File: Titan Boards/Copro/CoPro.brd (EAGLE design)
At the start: 101.6 x 101.6 mm, 83 parts, among them P2 RB1-125BAG1A, Q1 310mA/60V/1.6Ω, Q10 310mA/60V/1.6Ω, Q2 310mA/60V/1.6Ω, Q3 310mA/60V/1.6Ω, Q4 310mA/60V/1.6Ω, Q5 310mA/60V/1.6Ω, Q6 310mA/60V/1.6Ω, Q7 310mA/60V/1.6Ω, Q8 310mA/60V/1.6Ω, Q9 310mA/60V/1.6Ω, U1 SN74LVC3G04DCUT, U2 SN74LVC1G11DCKR, Y1 25Mhz, Y2 12MHz, Y3 32.768kHz

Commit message: Added My President Design to Board
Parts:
- moved PROGRAMMING1 3.81 mm to (6.35, 68.8)
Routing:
- net D-: track 43.7 -> 47.5 mm
- net D+: track 43.0 -> 46.8 mm
- net +3V3: track 414.6 -> 416.1 mm, vias 27 -> 28
- net BP_SDA: track 72.6 -> 73.9 mm
- net SWCLK: track 40.5 -> 39.9 mm, vias 2 -> 4
- net SPARE_8: track 56.8 -> 56.2 mm
- net 12V_ON/OFF: vias 3 -> 5
- net +5V: vias 8 -> 10

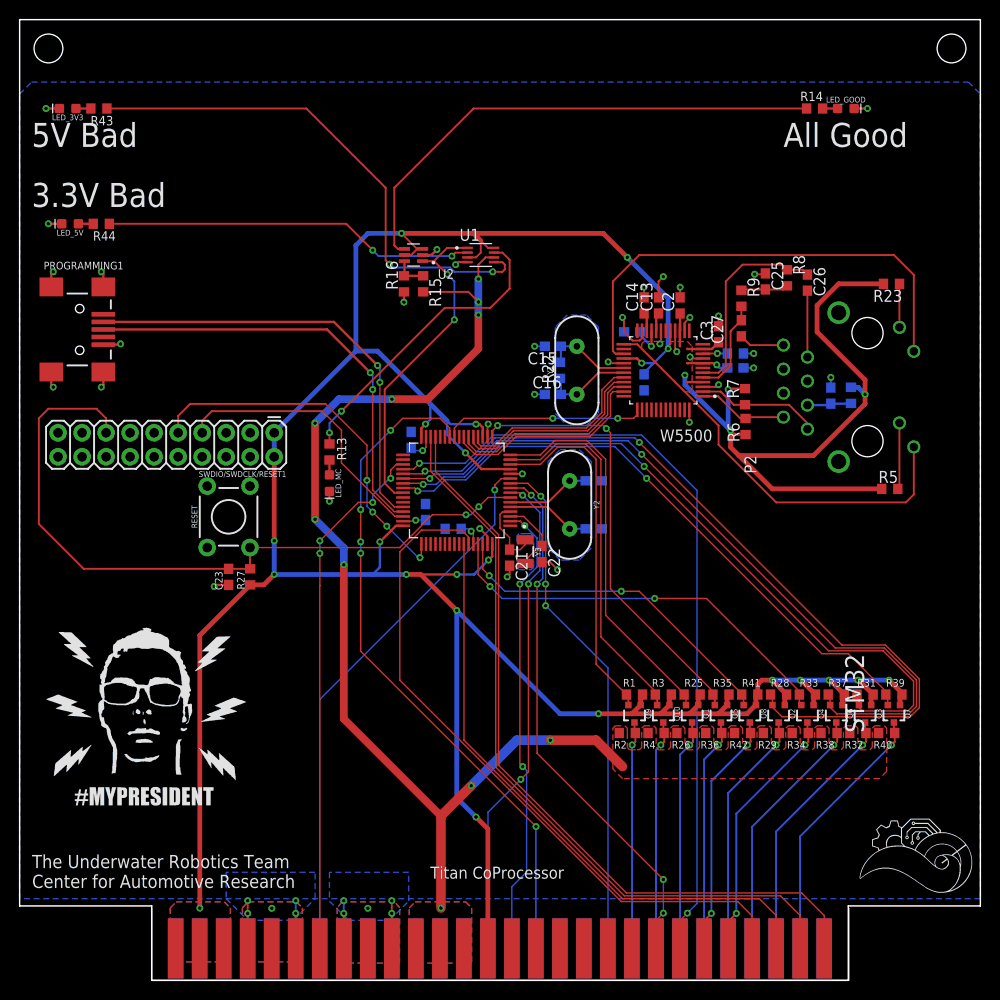
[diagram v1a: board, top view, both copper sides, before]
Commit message: CoPro - Increased some trace widths | Opened up ground plane | added decoupling capacitors to Main MicroController
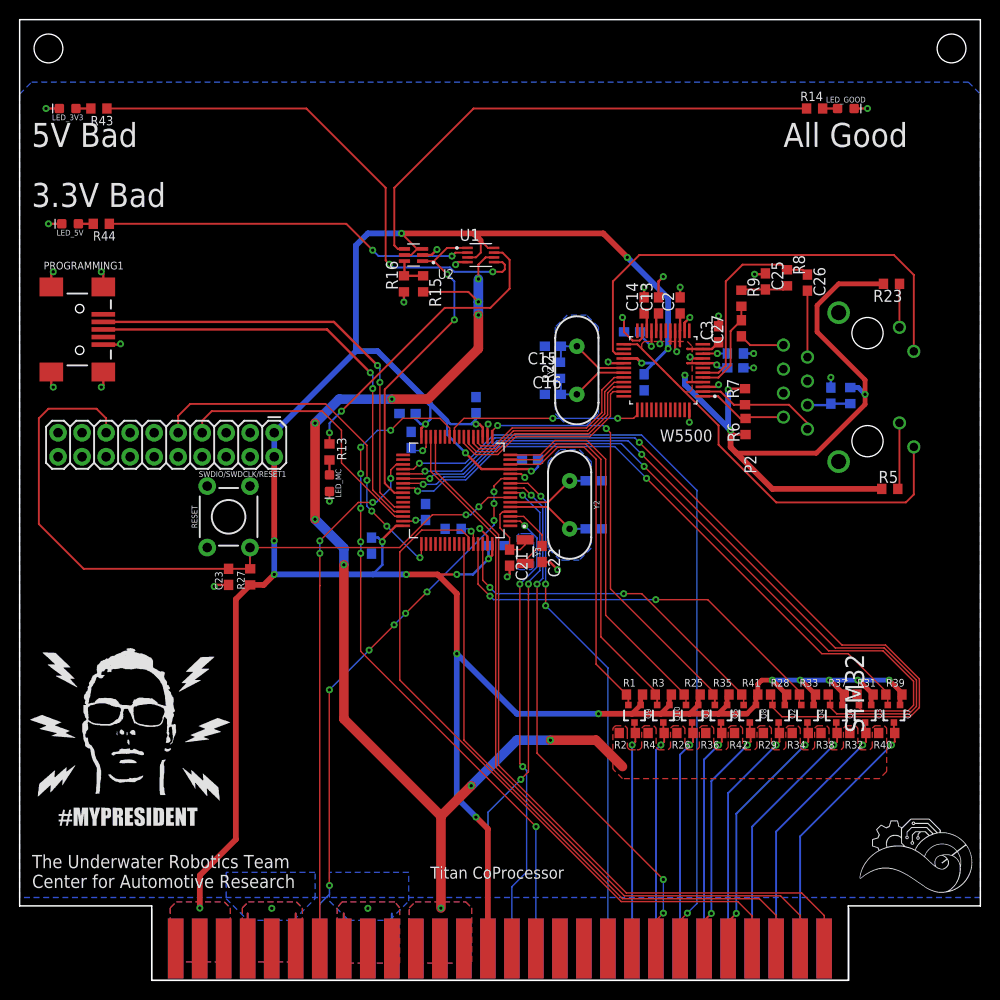
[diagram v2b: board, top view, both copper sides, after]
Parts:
- added C10, C11, C6, C8, C9: 0.1uF, rcl:C0603
- moved R10 0.08 mm to (87.8, 61.8)
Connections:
- net +3V3: now also C10.1, C11.1, C6.1, C8.1, C9.1
- net GND: now also C10.2, C11.2, C6.2, C8.2, C9.2
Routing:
- net GND: track 91.1 -> 80.3 mm, vias 44 -> 34
- net +3V3: track 416.1 -> 425.4 mm, vias 28 -> 29
- net 12V_ON/OFF: track 71.9 -> 72.7 mm, vias 5 -> 7
- net PWM_3V3_10: track 36.8 -> 37.5 mm
- net PWM_3V3_9: track 43.9 -> 44.5 mm
- net SPARE_1: vias 1 -> 9

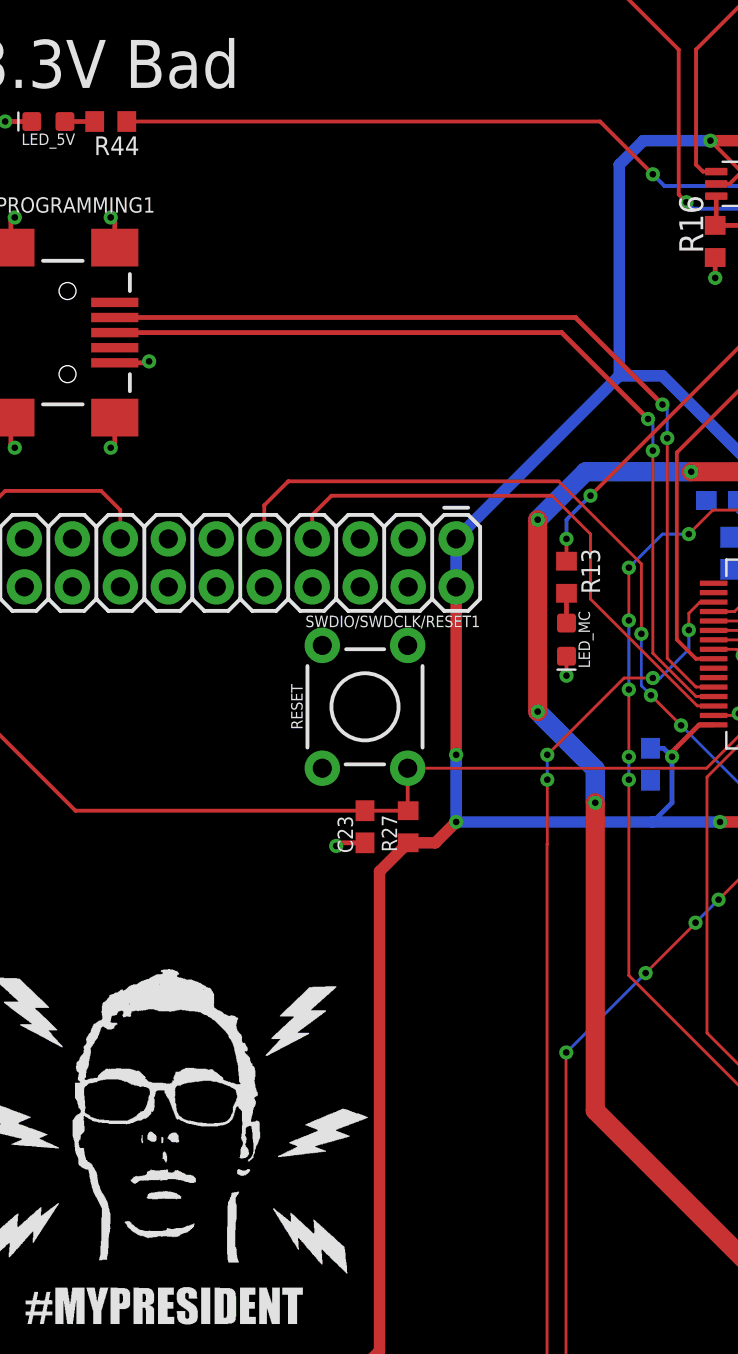
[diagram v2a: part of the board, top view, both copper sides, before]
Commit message: VBUS addition
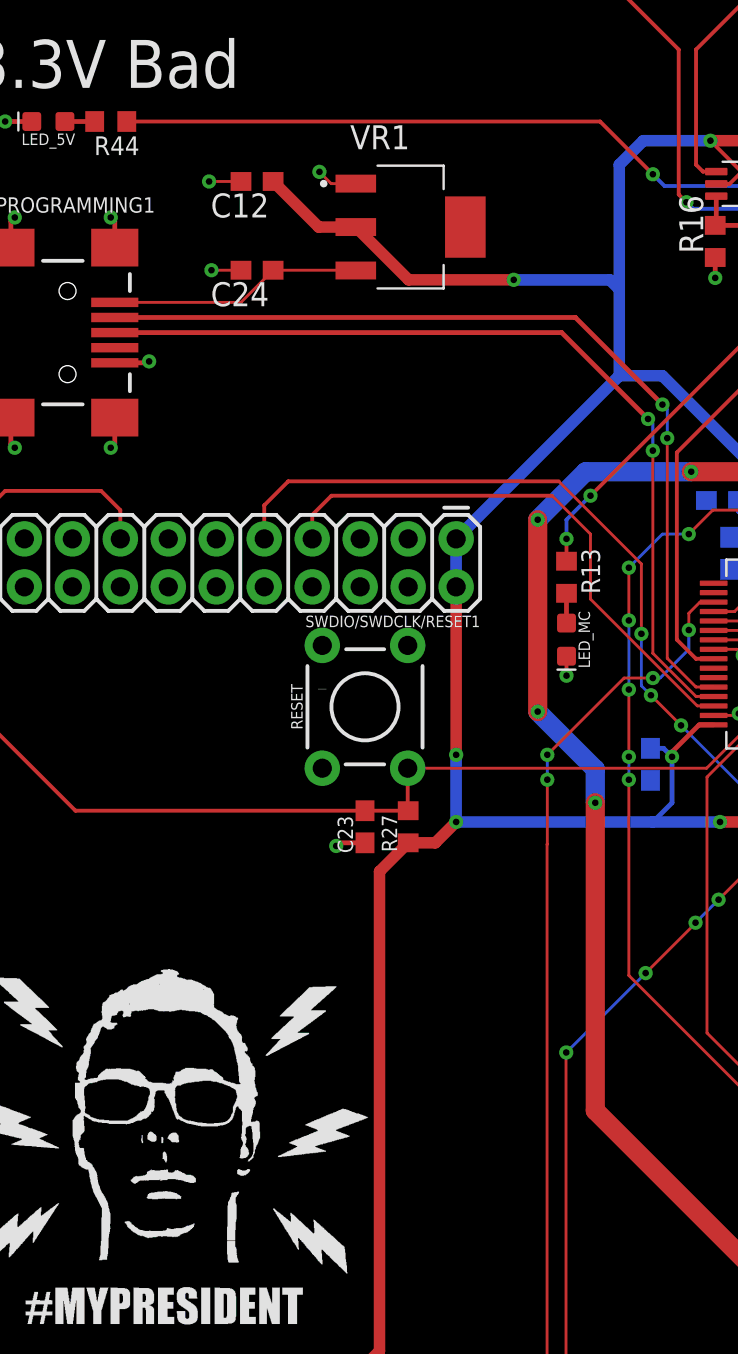
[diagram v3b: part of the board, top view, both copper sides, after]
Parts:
- added C12, C24: 10uF, rcl:C0603
- added VR1: LM1117IMPX-3.3/NOPB, LM1117IMPX-3.3_NOPB:VREG_LM1117IMPX-3.3/NOPB
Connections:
- net +3V3: now also C12.1, VR1.2
- net GND: now also C12.2, C24.2, VR1.1
- net VBUS: now also C24.1, VR1.3
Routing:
- net +3V3: track 425.4 -> 446.1 mm, vias 29 -> 30
- net VBUS: track 0.00 -> 13.5 mm
- net GND: track 80.3 -> 85.7 mm, vias 34 -> 37
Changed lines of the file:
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@@
 <?xml version="1.0" encoding="utf-8"?>
 <!DOCTYPE eagle SYSTEM "eagle.dtd">
-<eagle version="9.6.2">
+<eagle version="9.5.1">
 <drawing>
 <settings>
@@
 <layer number="128" name="_bValues" color="7" fill="1" visible="no" active="yes"/>
 <layer number="129" name="Mask" color="7" fill="1" visible="no" active="yes"/>
+<layer number="130" name="Boxes" color="4" fill="0" visible="yes" active="yes"/>
 <layer number="131" name="tAdjust" color="7" fill="1" visible="no" active="yes"/>
 <layer number="132" name="bAdjust" color="7" fill="1" visible="no" active="yes"/>
@@
 <rectangle x1="4.5085" y1="20.7391" x2="4.6101" y2="20.7645" layer="21"/>
 <rectangle x1="8.1407" y1="20.7391" x2="8.5217" y2="20.7645" layer="21"/>
-<rectangle x1="14.7955" y1="20.7391" x2="15.2273" y2="20.7645" layer="21"/>
+<rectangle x1="19.6215" y1="49.9491" x2="20.0533" y2="49.9745" layer="21"/>
 <rectangle x1="18.2499" y1="20.7391" x2="18.5547" y2="20.7645" layer="21"/>
 <rectangle x1="18.7325" y1="20.7391" x2="20.6375" y2="20.7645" layer="21"/>
@@
 <attribute name="VALUE" x="39.116" y="46.609" size="1.27" layer="28" rot="MR270"/>
 </element>
+<element name="VR1" library="LM1117IMPX-3.3_NOPB" package="VREG_LM1117IMPX-3.3/NOPB" value="LM1117IMPX-3.3/NOPB" x="24.511" y="74.422" smashed="yes">
+<attribute name="AVAILABILITY" value="Good" x="15.367" y="85.852" size="1.778" layer="27" display="off"/>
+<attribute name="DESCRIPTION" value=" 800-mA 15-V linear voltage regulator 4-SOT-223 -40 to 125 " x="15.367" y="85.852" size="1.778" layer="27" display="off"/>
+<attribute name="MF" value="Texas Instruments" x="15.367" y="85.852" size="1.778" layer="27" display="off"/>
+<attribute name="MP" value="LM1117IMPX-3.3/NOPB" x="15.367" y="85.852" size="1.778" layer="27" display="off"/>
+<attribute name="NAME" x="21.311" y="78.541" size="1.27" layer="25"/>
+<attribute name="PACKAGE" value="SOT-223-4 Texas Instruments" x="15.367" y="85.852" size="1.778" layer="27" display="off"/>
+<attribute name="PRICE" value="None" x="15.367" y="85.852" size="1.778" layer="27" display="off"/>
+<attribute name="PURCHASE-URL" value="https://pricing.snapeda.com/search/part/LM1117IMPX-3.3/NOPB/?ref=eda" x="15.367" y="85.852" size="1.778" layer="27" display="off"/>
+<attribute name="VALUE" x="21.311" y="70.692" size="1.27" layer="27" align="top-left"/>
+</element>
+<element name="C12" library="rcl" library_urn="urn:adsk.eagle:library:334" package="C0603" package3d_urn="urn:adsk.eagle:package:23616/2" value="10uF" x="16.383" y="76.835" smashed="yes" rot="R180">
+<attribute name="NAME" x="17.018" y="76.2" size="1.27" layer="25" rot="R180"/>
+<attribute name="POPULARITY" value="37" x="16.383" y="76.835" size="1.778" layer="27" rot="R180" display="off"/>
+<attribute name="SPICEPREFIX" value="C" x="16.383" y="76.835" size="1.778" layer="27" rot="R180" display="off"/>
+<attribute name="VALUE" x="17.018" y="78.74" size="1.27" layer="27" rot="R180"/>
+</element>
+<element name="C24" library="rcl" library_urn="urn:adsk.eagle:library:334" package="C0603" package3d_urn="urn:adsk.eagle:package:23616/2" value="10uF" x="16.383" y="72.136" smashed="yes" rot="R180">
+<attribute name="NAME" x="17.018" y="71.501" size="1.27" layer="25" rot="R180"/>
+<attribute name="POPULARITY" value="37" x="16.383" y="72.136" size="1.778" layer="27" rot="R180" display="off"/>
+<attribute name="SPICEPREFIX" value="C" x="16.383" y="72.136" size="1.778" layer="27" rot="R180" display="off"/>
+<attribute name="VALUE" x="17.018" y="74.041" size="1.27" layer="27" rot="R180"/>
+</element>
 </elements>
 <signals>
@@
 <contactref element="C9" pad="2"/>
 <contactref element="C10" pad="2"/>
+<contactref element="C24" pad="2"/>
+<contactref element="VR1" pad="1"/>
+<contactref element="C12" pad="2"/>
+<wire x1="21.611" y1="76.722" x2="20.306" y2="76.722" width="0.1524" layer="1"/>
+<wire x1="20.306" y1="76.722" x2="19.685" y2="77.343" width="0.1524" layer="1"/>
+<via x="19.685" y="77.343" extent="1-16" drill="0.35"/>
+<wire x1="15.533" y1="76.835" x2="13.843" y2="76.835" width="0.1524" layer="1"/>
+<via x="13.843" y="76.835" extent="1-16" drill="0.35"/>
+<wire x1="15.533" y1="72.136" x2="13.97" y2="72.136" width="0.1524" layer="1"/>
+<via x="13.97" y="72.136" extent="1-16" drill="0.35"/>
 </signal>
 <signal name="+5V">
@@
 <wire x1="26.924" y1="55.372" x2="26.924" y2="57.912" width="0.6096" layer="16"/>
 <wire x1="26.924" y1="57.912" x2="35.56" y2="66.548" width="0.6096" layer="16"/>
-<wire x1="35.56" y1="77.724" x2="35.56" y2="66.548" width="0.6096" layer="16"/>
+<wire x1="35.56" y1="77.724" x2="35.56" y2="71.12" width="0.6096" layer="16"/>
+<wire x1="35.56" y1="71.12" x2="35.56" y2="66.548" width="0.6096" layer="16"/>
 <wire x1="35.56" y1="66.548" x2="37.846" y2="66.548" width="0.6096" layer="16"/>
 <wire x1="37.846" y1="66.548" x2="43.434" y2="60.96" width="0.6096" layer="16"/>
@@
 <wire x1="54.825" y1="54.317" x2="54.356" y2="53.848" width="0.254" layer="16"/>
 <wire x1="54.825" y1="54.317" x2="54.825" y2="55.118" width="0.254" layer="16"/>
+<contactref element="VR1" pad="2"/>
+<contactref element="C12" pad="1"/>
+<wire x1="35.56" y1="71.12" x2="35.052" y2="71.628" width="0.6096" layer="16"/>
+<wire x1="35.052" y1="71.628" x2="29.972" y2="71.628" width="0.6096" layer="16"/>
+<via x="29.972" y="71.628" extent="1-16" drill="0.35"/>
+<wire x1="29.972" y1="71.628" x2="24.405" y2="71.628" width="0.6096" layer="1"/>
+<wire x1="24.405" y1="71.628" x2="21.611" y2="74.422" width="0.6096" layer="1"/>
+<wire x1="21.611" y1="74.422" x2="19.646" y2="74.422" width="0.6096" layer="1"/>
+<wire x1="19.646" y1="74.422" x2="17.233" y2="76.835" width="0.6096" layer="1"/>
 </signal>
 <signal name="BP_SDA">
@@
 <signal name="VBUS">
 <contactref element="PROGRAMMING1" pad="VBUS"/>
+<contactref element="VR1" pad="3"/>
+<contactref element="C24" pad="1"/>
+<wire x1="8.85" y1="70.434" x2="15.531" y2="70.434" width="0.1524" layer="1"/>
+<wire x1="15.531" y1="70.434" x2="17.233" y2="72.136" width="0.1524" layer="1"/>
+<wire x1="17.233" y1="72.136" x2="21.597" y2="72.136" width="0.1524" layer="1"/>
+<wire x1="21.597" y1="72.136" x2="21.611" y2="72.122" width="0.1524" layer="1"/>
 </signal>
 </signals>

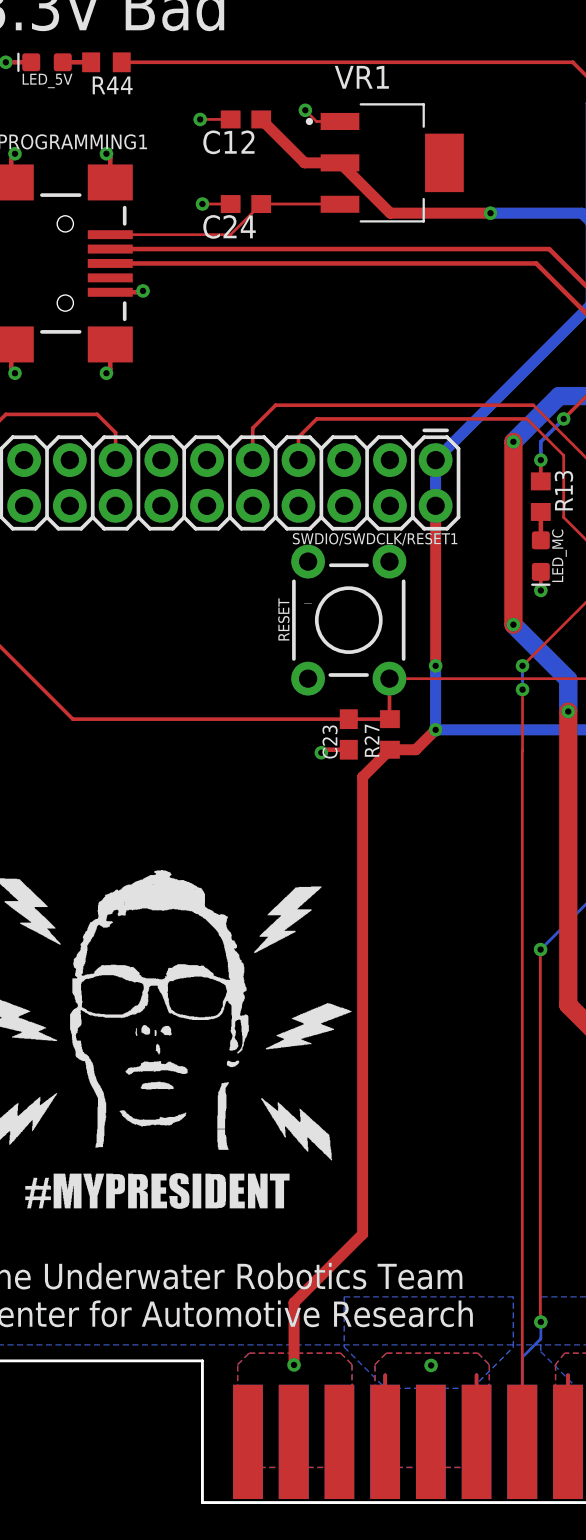
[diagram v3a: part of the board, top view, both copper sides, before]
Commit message: Increased some trace widths
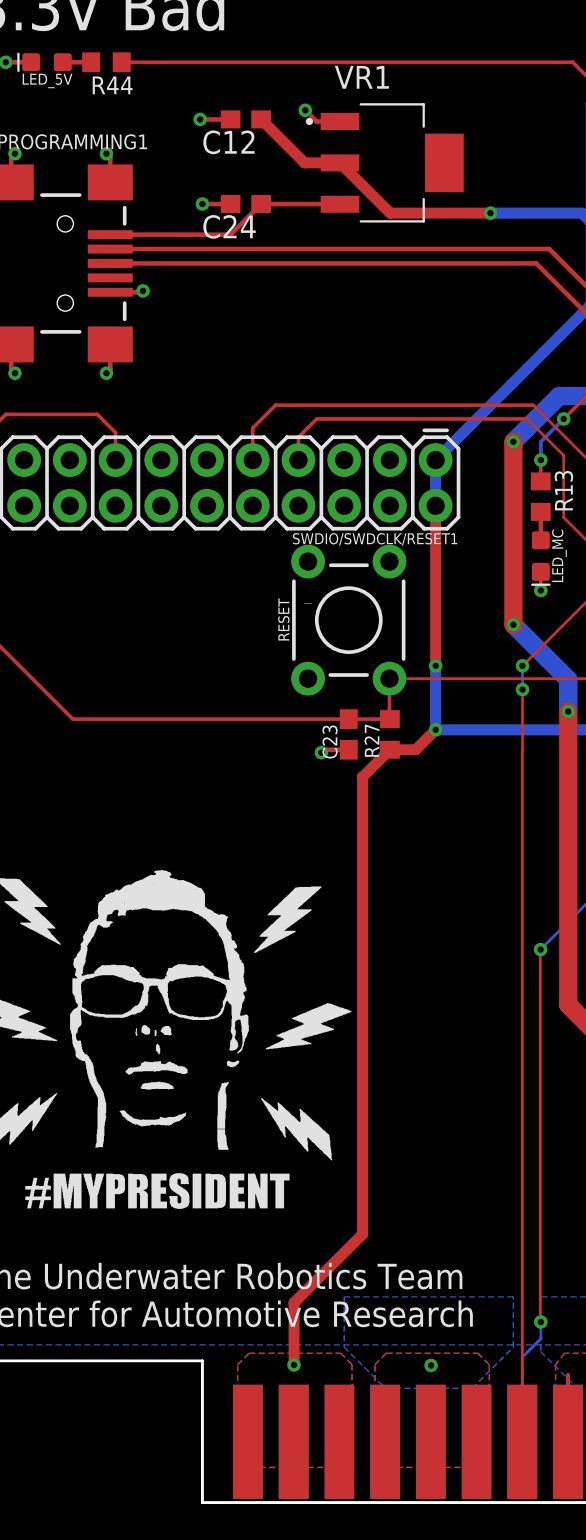
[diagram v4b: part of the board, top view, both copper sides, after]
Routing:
- net GND: track 85.7 -> 70.9 mm
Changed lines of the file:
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@@
 <?xml version="1.0" encoding="utf-8"?>
 <!DOCTYPE eagle SYSTEM "eagle.dtd">
-<eagle version="9.5.1">
+<eagle version="9.6.2">
 <drawing>
 <settings>
@@
 <wire x1="53.0366" y1="53.566" x2="51.898" y2="53.566" width="0.2032" layer="1"/>
 <wire x1="76.542" y1="66.294" x2="77.6226" y2="66.294" width="0.254" layer="16"/>
-<wire x1="24.1173" y1="3.375" x2="24.1173" y2="7.0806" width="0.2032" layer="16"/>
-<wire x1="24.1173" y1="3.375" x2="24.1173" y2="7.0806" width="0.2032" layer="1"/>
-<wire x1="29.1973" y1="3.375" x2="29.1973" y2="7.0806" width="0.2032" layer="1"/>
-<wire x1="29.1973" y1="3.375" x2="29.1973" y2="7.0806" width="0.2032" layer="16"/>
 <wire x1="34.2773" y1="3.375" x2="34.2773" y2="7.0806" width="0.2032" layer="1"/>
 <wire x1="34.2773" y1="3.375" x2="34.2773" y2="7.0806" width="0.2032" layer="16"/>
@@
 <contactref element="VR1" pad="1"/>
 <contactref element="C12" pad="2"/>
-<wire x1="21.611" y1="76.722" x2="20.306" y2="76.722" width="0.1524" layer="1"/>
-<wire x1="20.306" y1="76.722" x2="19.685" y2="77.343" width="0.1524" layer="1"/>
+<wire x1="21.611" y1="76.722" x2="20.306" y2="76.722" width="0.254" layer="1"/>
+<wire x1="20.306" y1="76.722" x2="19.685" y2="77.343" width="0.254" layer="1"/>
 <via x="19.685" y="77.343" extent="1-16" drill="0.35"/>
-<wire x1="15.533" y1="76.835" x2="13.843" y2="76.835" width="0.1524" layer="1"/>
+<wire x1="15.533" y1="76.835" x2="13.843" y2="76.835" width="0.254" layer="1"/>
 <via x="13.843" y="76.835" extent="1-16" drill="0.35"/>
-<wire x1="15.533" y1="72.136" x2="13.97" y2="72.136" width="0.1524" layer="1"/>
+<wire x1="15.533" y1="72.136" x2="13.97" y2="72.136" width="0.254" layer="1"/>
 <via x="13.97" y="72.136" extent="1-16" drill="0.35"/>
 </signal>
@@
 <contactref element="VR1" pad="3"/>
 <contactref element="C24" pad="1"/>
-<wire x1="8.85" y1="70.434" x2="15.531" y2="70.434" width="0.1524" layer="1"/>
-<wire x1="15.531" y1="70.434" x2="17.233" y2="72.136" width="0.1524" layer="1"/>
-<wire x1="17.233" y1="72.136" x2="21.597" y2="72.136" width="0.1524" layer="1"/>
+<wire x1="8.85" y1="70.434" x2="15.531" y2="70.434" width="0.254" layer="1"/>
+<wire x1="15.531" y1="70.434" x2="17.233" y2="72.136" width="0.254" layer="1"/>
+<wire x1="17.233" y1="72.136" x2="21.597" y2="72.136" width="0.254" layer="1"/>
 <wire x1="21.597" y1="72.136" x2="21.611" y2="72.122" width="0.1524" layer="1"/>
 </signal>
